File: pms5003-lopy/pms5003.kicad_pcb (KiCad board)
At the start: 2 copper layers, 55 x 60 mm, 11 parts, among them J1 Battery, J2 DS3231, J3 PMS5003, J4 SHT10, J5 P2, J6 PROG, Q1 IRF540N, U1 U3V12F5, U11 LoPy4

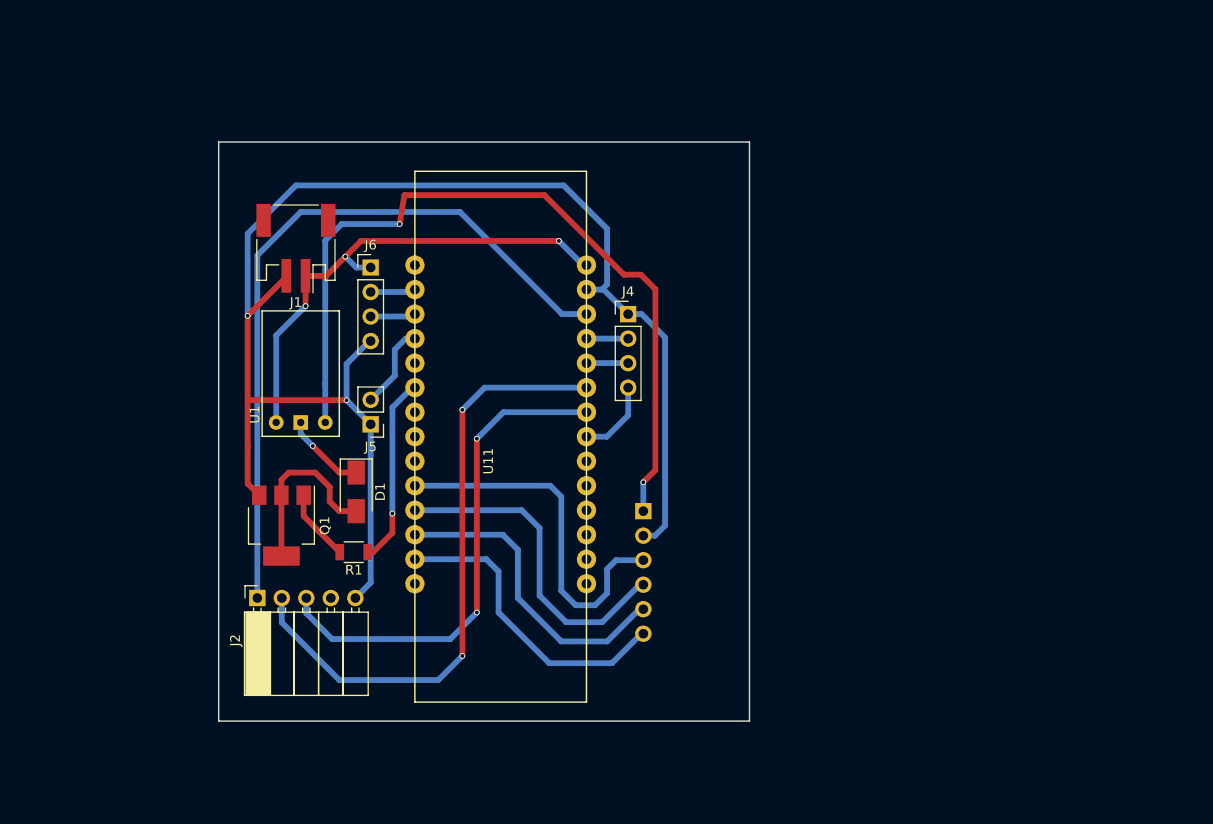
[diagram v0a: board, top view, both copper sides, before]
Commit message: PMS5003: Add battery charger circuit
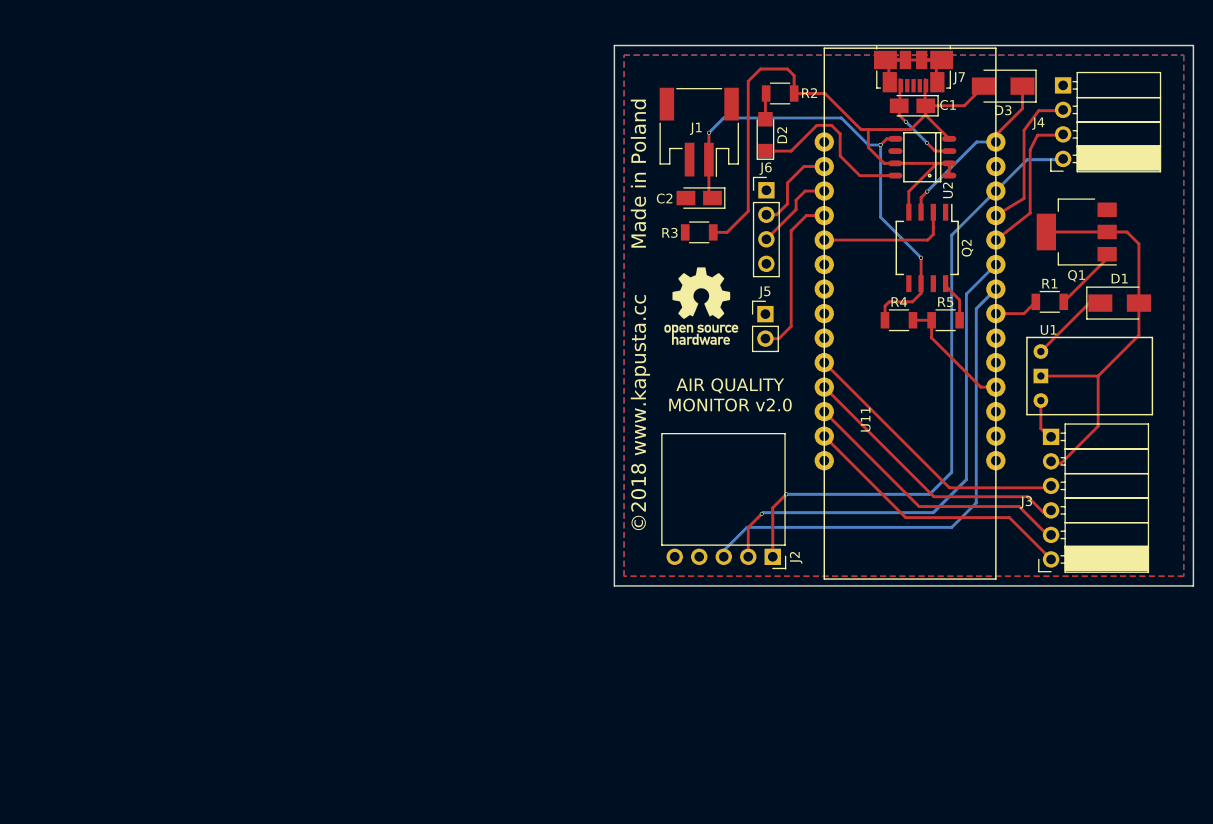
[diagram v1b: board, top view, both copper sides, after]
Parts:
- added C1: 4.7uF, Capacitors_Tantalum_SMD:CP_Tantalum_Case-A_EIA-3216-18_Reflow, F.Cu at (151.9, 31.2)
- added C2: 10uF, Capacitors_Tantalum_SMD:CP_Tantalum_Case-A_EIA-3216-18_Reflow, F.Cu at (129.8, 40.8)
- added D2: LED, LEDs:LED_1206, F.Cu at (136.7, 34.3)
- added D3: D_Schottky, Diodes_SMD:D_SMA, F.Cu at (161.3, 29.2)
- added J7: USB_OTG, Connectors_USB:USB_Micro-B_Molex_47346-0001, F.Cu at (152.0, 26.5)
- added Q2: IRF7309IPBF, Housings_SOIC:SO-8_5.3x6.2mm_Pitch1.27mm, F.Cu at (153.4, 46.0)
- added R2: 100, Resistors_SMD:R_1206, F.Cu at (138.2, 30.0)
- added R3: 100k, Resistors_SMD:R_1206, F.Cu at (129.8, 44.4)
- added R4: 100k, Resistors_SMD:R_1206, F.Cu at (150.5, 53.5)
- added R5: 47k, Resistors_SMD:R_1206, F.Cu at (155.3, 53.5)
- added REF***: OSHW-Logo_7.5x8mm_SilkScreen, Symbols:OSHW-Logo_7.5x8mm_SilkScreen, F.Cu at (130.0, 52.0)
- added U2: MAX1811, Power_Integrations:SO-8, F.Cu at (152.9, 36.6)
- J2: footprint Socket_Strips:Socket_Strip_Angled_1x05_Pitch2.54mm -> various:DS3231
- J3: footprint Socket_Strips:Socket_Strip_Angled_1x06_Pitch2.54mm -> PMS5003; moved to F.Cu
- J4: footprint Socket_Strips:Socket_Strip_Straight_1x04_Pitch2.54mm -> SHT10
- J5: footprint Socket_Strips:Socket_Strip_Straight_1x02_Pitch2.54mm -> Pin_Headers:Pin_Header_Straight_1x02_Pitch2.54mm
- J6: footprint Socket_Strips:Socket_Strip_Straight_1x04_Pitch2.54mm -> Pin_Headers:Pin_Header_Straight_1x04_Pitch2.54mm
- R1: value R -> 100
- moved U1 92.3 mm to (176.8, 55.2), turned to 180 degrees
- moved Q1 87.8 mm to (168.9, 44.3), turned to 180 degrees
- moved D1 81.5 mm to (173.4, 51.7), turned to 0 degrees
- moved R1 76.6 mm to (166.1, 51.6), turned to 0 degrees
- moved J2 53.6 mm to (137.4, 78.0), turned to 270 degrees
- moved J4 47.9 mm to (167.5, 36.8), turned to 180 degrees
- moved U11 44.3 mm to (142.8, 35.0)
- moved J1 43.5 mm to (129.8, 33.9)
- moved J3 42.5 mm to (166.2, 78.2)
- moved J5 42.5 mm to (136.7, 52.8), turned to 0 degrees
- moved J6 41.8 mm to (136.8, 40.0)
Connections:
- D1 pad 1: Net-(D1-Pad1) -> VCC
- D1 pad 2: Net-(D1-Pad2) -> 5V_GND
- J1 pad 1: VCC -> VBATT+
- J1 pad 2: GND -> -USB
- J2 pad 5: GND -> -USB
- J3 pad 2: GND -> 5V_GND
- J4 pad 1: GND -> -USB
- J4 pad 4: SHT10_VCC -> 3V3
- J5 pad 1: GND -> -USB
- J6 pad 4: GND -> -USB
- Q1 pad 2: Net-(D1-Pad2) -> 5V_GND
- Q1 pad 3: GND -> -USB
- U1 pad 2: Net-(D1-Pad1) -> 5V_GND
- U11 pad 18: (no net) -> ADC
- U11 pad 21: SHT10_VCC -> PMS_EN
- U11 pad 27: GND -> -USB
- U11 pad 5: (no net) -> ADC_EN
- U11 pad 6: PMS_EN -> (no net)
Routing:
- net GND: track 153.1 -> 0.00 mm, vias 2 -> 0
- net 5V: track 83.9 -> 4.40 mm, vias 2 -> 0
- net +USB: track 0.00 -> 73.8 mm
- net VBATT+: track 0.00 -> 51.1 mm, vias 0 -> 3
- net 5V_GND: track 0.00 -> 43.2 mm
- net VCC: track 51.2 -> 27.7 mm, vias 3 -> 1
- net Net-(D1-Pad2): track 18.5 -> 0.00 mm
- net Net-(D2-Pad1): track 0.00 -> 18.1 mm
- net Net-(J7-Pad6): track 0.00 -> 14.9 mm
- net PMS_EN: track 19.6 -> 5.51 mm, vias 1 -> 0
- net ADC_EN: track 0.00 -> 13.9 mm
- net RTC_SDA: track 64.1 -> 51.2 mm, vias 2 -> 1
- net ADC: track 0.00 -> 12.5 mm
- net 3V3: track 75.9 -> 64.5 mm, vias 0 -> 1
- net SHT10_DATA: track 4.32 -> 15.5 mm
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- added copper zone on F.Cu, net -USB
- added copper zone on B.Cu, net VCC
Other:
- board size 55 x 60 mm -> 60 x 56 mm
- net class Default: clearance 0.3 -> 0.2; trace_width 0.6 -> 0.3; via_dia 0.6 -> 0.4; via_drill 0.4 -> 0.3
- rule trace_clearance: 0.3 -> 0.2
- rule trace_min: 0.6 -> 0.3
- board text added: "AIR QUALITY MONITOR v2.0"
- board text added: "©2018 www.kapusta.cc Made in Poland"

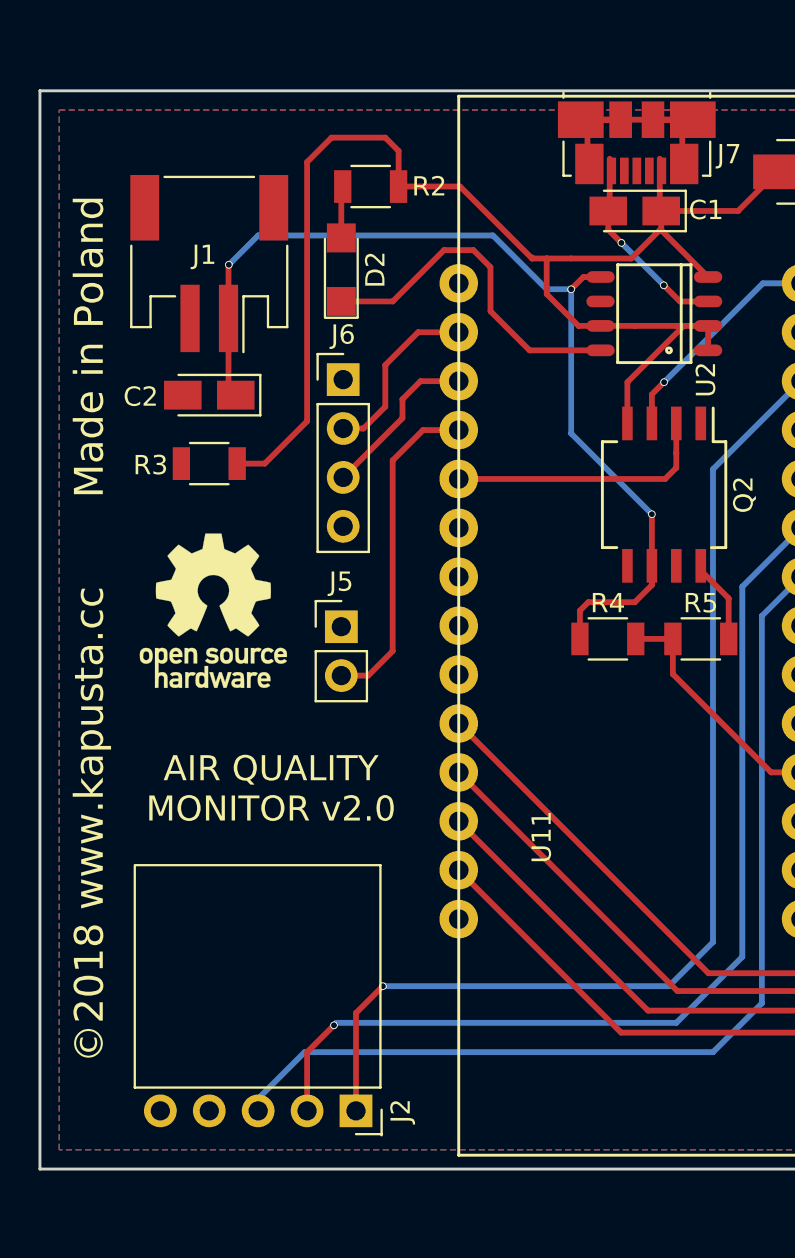
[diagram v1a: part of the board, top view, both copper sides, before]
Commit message: Add W01-based PMS5003 board
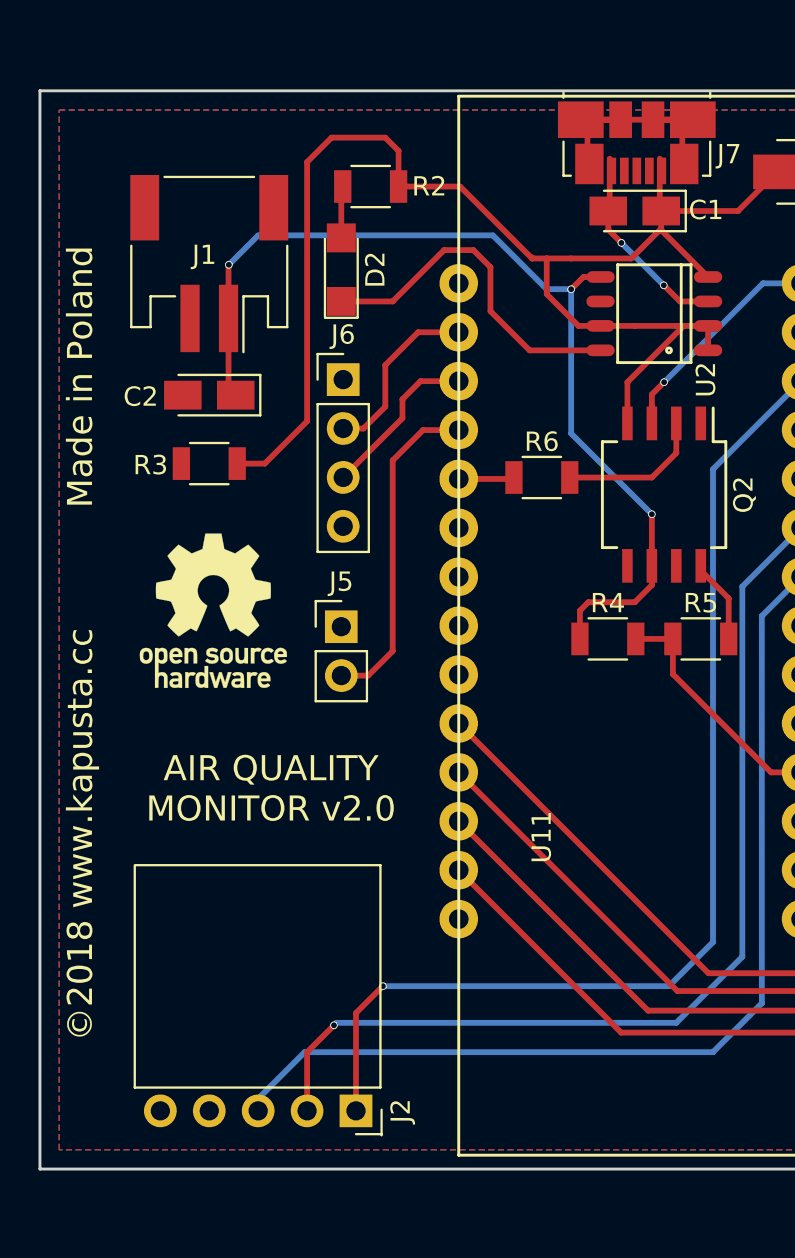
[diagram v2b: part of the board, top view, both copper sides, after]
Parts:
- added R6: 100, Resistors_SMD:R_1206, F.Cu at (147.1, 45.1)
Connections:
- Q2 pad 2: ADC_EN -> Net-(Q2-Pad2)
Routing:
- net ADC_EN: track 13.9 -> 2.90 mm
- net Net-(Q2-Pad2): track 0.00 -> 7.62 mm
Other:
- board text added: "Prasłowiańska grusza chroni w swych konarach plebejskiego uciekiniera"
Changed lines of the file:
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@@
 (kicad_pcb (version 4) (host pcbnew 4.0.7)
   (general
-    (links 61)
+    (links 62)
     (no_connects 0)
-    (area 120.924999 24.924999 181.075001 81.075001)
+    (area 104.650001 18.3 181.075001 87.700001)
     (thickness 1.6)
-    (drawings 10)
-    (tracks 180)
+    (drawings 11)
+    (tracks 181)
     (zones 0)
-    (modules 23)
-    (nets 27)
+    (modules 24)
+    (nets 28)
   )
   (page A4)
@@
     (visible_elements FFFFFF7F)
     (pcbplotparams
-      (layerselection 0x00030_80000001)
-      (usegerberextensions false)
+      (layerselection 0x010f0_80000001)
+      (usegerberextensions true)
       (excludeedgelayer true)
       (linewidth 0.100000)
@@
       (outputformat 1)
       (mirror false)
-      (drillshape 1)
+      (drillshape 0)
       (scaleselection 1)
-      (outputdirectory ""))
+      (outputdirectory gerber/))
   )
   (net 0 "")
@@
   (net 25 ADC)
   (net 26 "Net-(J7-Pad6)")
+  (net 27 "Net-(Q2-Pad2)")
   (net_class Default "This is the default net class."
     (clearance 0.2)
@@
     (add_net "Net-(J7-Pad6)")
     (add_net "Net-(Q1-Pad1)")
+    (add_net "Net-(Q2-Pad2)")
     (add_net "Net-(Q2-Pad8)")
     (add_net P2)
@@
       (net 19 -USB))
     (pad 2 smd rect (at -3.7 -0.635 270) (size 1.75 0.55) (layers F.Cu F.Paste F.Mask)
-      (net 23 ADC_EN))
+      (net 27 "Net-(Q2-Pad2)"))
     (pad 3 smd rect (at -3.7 0.635 270) (size 1.75 0.55) (layers F.Cu F.Paste F.Mask)
       (net 1 VCC))
@@
     )
   )
-  (gr_text "©2018 www.kapusta.cc       Made in Poland" (at 123.571 52.959 90) (layer F.SilkS)
-    (effects (font (size 1.5 1.5) (thickness 0.3)))
+  (module Resistors_SMD:R_1206 (layer F.Cu)
+    (at 147.066 45.085)
+    (descr "Resistor SMD 1206, reflow soldering, Vishay (see dcrcw.pdf)")
+    (tags "resistor 1206")
+    (attr smd)
+    (fp_text reference R6 (at 0 -1.85) (layer F.SilkS)
+      (effects (font (size 1 1) (thickness 0.15)))
+    )
+    (fp_text value 100 (at 0 1.95) (layer F.Fab)
+      (effects (font (size 1 1) (thickness 0.15)))
+    )
+    (fp_text user %R (at 0 0) (layer F.Fab)
+      (effects (font (size 0.7 0.7) (thickness 0.105)))
+    )
+    (fp_line (start -1.6 0.8) (end -1.6 -0.8) (layer F.Fab) (width 0.1))
+    (fp_line (start 1.6 0.8) (end -1.6 0.8) (layer F.Fab) (width 0.1))
+    (fp_line (start 1.6 -0.8) (end 1.6 0.8) (layer F.Fab) (width 0.1))
+    (fp_line (start -1.6 -0.8) (end 1.6 -0.8) (layer F.Fab) (width 0.1))
+    (fp_line (start 1 1.07) (end -1 1.07) (layer F.SilkS) (width 0.12))
+    (fp_line (start -1 -1.07) (end 1 -1.07) (layer F.SilkS) (width 0.12))
+    (fp_line (start -2.15 -1.11) (end 2.15 -1.11) (layer F.CrtYd) (width 0.05))
+    (fp_line (start -2.15 -1.11) (end -2.15 1.1) (layer F.CrtYd) (width 0.05))
+    (fp_line (start 2.15 1.1) (end 2.15 -1.11) (layer F.CrtYd) (width 0.05))
+    (fp_line (start 2.15 1.1) (end -2.15 1.1) (layer F.CrtYd) (width 0.05))
+    (pad 1 smd rect (at -1.45 0) (size 0.9 1.7) (layers F.Cu F.Paste F.Mask)
+      (net 23 ADC_EN))
+    (pad 2 smd rect (at 1.45 0) (size 0.9 1.7) (layers F.Cu F.Paste F.Mask)
+      (net 27 "Net-(Q2-Pad2)"))
+    (model ${KISYS3DMOD}/Resistors_SMD.3dshapes/R_1206.wrl
+      (at (xyz 0 0 0))
+      (scale (xyz 1 1 1))
+      (rotate (xyz 0 0 0))
+    )
+  )
+  (gr_text "Prasłowiańska grusza chroni w swych konarach plebejskiego uciekiniera" (at 151.05 79.9) (layer B.SilkS)
+    (effects (font (size 1 1) (thickness 0.2)) (justify mirror))
+  )
+  (gr_text "©2018 www.kapusta.cc           Made in Poland" (at 123.1 53.7 90) (layer F.SilkS)
+    (effects (font (size 1.3 1.3) (thickness 0.25)))
   )
   (dimension 14 (width 0.3) (layer Cmts.User)
@@
   (segment (start 171.355 51.689) (end 170.2145 51.689) (width 0.3) (layer F.Cu) (net 1))
   (segment (start 170.2145 51.689) (end 165.193 56.7105) (width 0.3) (layer F.Cu) (net 1))
-  (segment (start 167.42 36.83) (end 163.78 36.83) (width 0.3) (layer B.Cu) (net 2) (status 400000))
+  (segment (start 167.42 36.83) (end 163.78 36.83) (width 0.3) (layer B.Cu) (net 2))
   (segment (start 163.78 36.83) (end 160.53 40.08) (width 0.3) (layer B.Cu) (net 2))
-  (segment (start 167.42 36.83) (end 167.5 36.75) (width 0.3) (layer B.Cu) (net 2) (status C00000))
+  (segment (start 167.42 36.83) (end 167.5 36.75) (width 0.3) (layer B.Cu) (net 2))
   (segment (start 155.956 44.654) (end 160.53 40.08) (width 0.3) (layer B.Cu) (net 2))
   (segment (start 137.414 77.978) (end 137.414 72.898) (width 0.3) (layer F.Cu) (net 2))
@@
   (segment (start 167.259 31.75) (end 164.973 31.75) (width 0.3) (layer F.Cu) (net 10))
   (segment (start 164.973 31.75) (end 163.449 33.782) (width 0.3) (layer F.Cu) (net 10))
-  (segment (start 167.42 34.29) (end 164.846 34.29) (width 0.3) (layer F.Cu) (net 11) (status 400000))
+  (segment (start 167.42 34.29) (end 164.846 34.29) (width 0.3) (layer F.Cu) (net 11))
   (segment (start 164.846 34.29) (end 164.084 35.814) (width 0.3) (layer F.Cu) (net 11))
   (segment (start 164.084 35.814) (end 164.084 42.368) (width 0.3) (layer F.Cu) (net 11))
   (segment (start 164.084 42.368) (end 160.53 45.16) (width 0.3) (layer F.Cu) (net 11))
-  (segment (start 167.42 34.29) (end 167.5 34.21) (width 0.3) (layer F.Cu) (net 11) (status C00000))
+  (segment (start 167.42 34.29) (end 167.5 34.21) (width 0.3) (layer F.Cu) (net 11))
   (segment (start 172.06 46.623) (end 172.06 47.068) (width 0.3) (layer F.Cu) (net 12))
   (segment (start 172.06 47.068) (end 167.566 51.562) (width 0.3) (layer F.Cu) (net 12))
@@
   (segment (start 139.32 35.94) (end 136.652 35.94) (width 0.3) (layer F.Cu) (net 22))
   (segment (start 141.986 33.274) (end 139.32 35.94) (width 0.3) (layer F.Cu) (net 22))
-  (segment (start 154.051 43.815) (end 154.051 42.274) (width 0.3) (layer F.Cu) (net 23))
-  (segment (start 154.051 43.798) (end 154.051 43.815) (width 0.3) (layer F.Cu) (net 23))
-  (segment (start 154.051 43.815) (end 154.051 44.577) (width 0.3) (layer F.Cu) (net 23))
-  (segment (start 154.051 44.577) (end 153.468 45.16) (width 0.3) (layer F.Cu) (net 23))
-  (segment (start 153.468 45.16) (end 142.75 45.16) (width 0.3) (layer F.Cu) (net 23))
+  (segment (start 142.75 45.16) (end 145.541 45.16) (width 0.3) (layer F.Cu) (net 23))
+  (segment (start 145.541 45.16) (end 145.616 45.085) (width 0.3) (layer F.Cu) (net 23))
   (segment (start 155.321 49.674) (end 155.321 49.911) (width 0.3) (layer F.Cu) (net 24))
   (segment (start 155.321 49.911) (end 156.771 51.361) (width 0.3) (layer F.Cu) (net 24))
@@
   (segment (start 153.871 55.2936) (end 158.9774 60.4) (width 0.3) (layer F.Cu) (net 25))
   (segment (start 153.871 53.467) (end 151.945 53.467) (width 0.3) (layer F.Cu) (net 25))
-  (segment (start 152.84 26.5) (end 154.91 26.5) (width 0.3) (layer F.Cu) (net 26) (status C00000))
-  (segment (start 149.09 26.5) (end 151.16 26.5) (width 0.3) (layer F.Cu) (net 26) (status C00000))
-  (segment (start 149.09 26.5) (end 154.91 26.5) (width 0.3) (layer F.Cu) (net 26) (status C00000))
+  (segment (start 152.84 26.5) (end 154.91 26.5) (width 0.3) (layer F.Cu) (net 26))
+  (segment (start 149.09 26.5) (end 151.16 26.5) (width 0.3) (layer F.Cu) (net 26))
+  (segment (start 149.09 26.5) (end 154.91 26.5) (width 0.3) (layer F.Cu) (net 26))
   (segment (start 149.4375 28.2) (end 149.4375 26.3475) (width 0.3) (layer F.Cu) (net 26))
   (segment (start 149.4375 26.3475) (end 149.885 25.9) (width 0.3) (layer F.Cu) (net 26))
   (segment (start 154.81 25.9) (end 154.3625 26.3475) (width 0.3) (layer F.Cu) (net 26))
   (segment (start 154.3625 26.3475) (end 154.3625 28.2) (width 0.3) (layer F.Cu) (net 26))
+  (segment (start 148.516 45.085) (end 152.781 45.085) (width 0.3) (layer F.Cu) (net 27))
+  (segment (start 152.781 45.085) (end 154.051 43.815) (width 0.3) (layer F.Cu) (net 27))
+  (segment (start 154.051 43.815) (end 154.051 42.274) (width 0.3) (layer F.Cu) (net 27))
+  (segment (start 154.051 43.798) (end 154.051 43.815) (width 0.3) (layer F.Cu) (net 27))
   (zone (net 19) (net_name -USB) (layer F.Cu) (hatch edge 0.508)
     (connect_pads (clearance 0.508))
